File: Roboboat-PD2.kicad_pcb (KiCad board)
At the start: 2 copper layers, 78 x 60.7 mm, 44 parts, among them J1 14.4V, J10 Motor, J11 Motor, J12 Motor, J13 Motor, J14 Motor, J15 Motor, J16 Motor, J17 GND TP, J2 PGOOD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

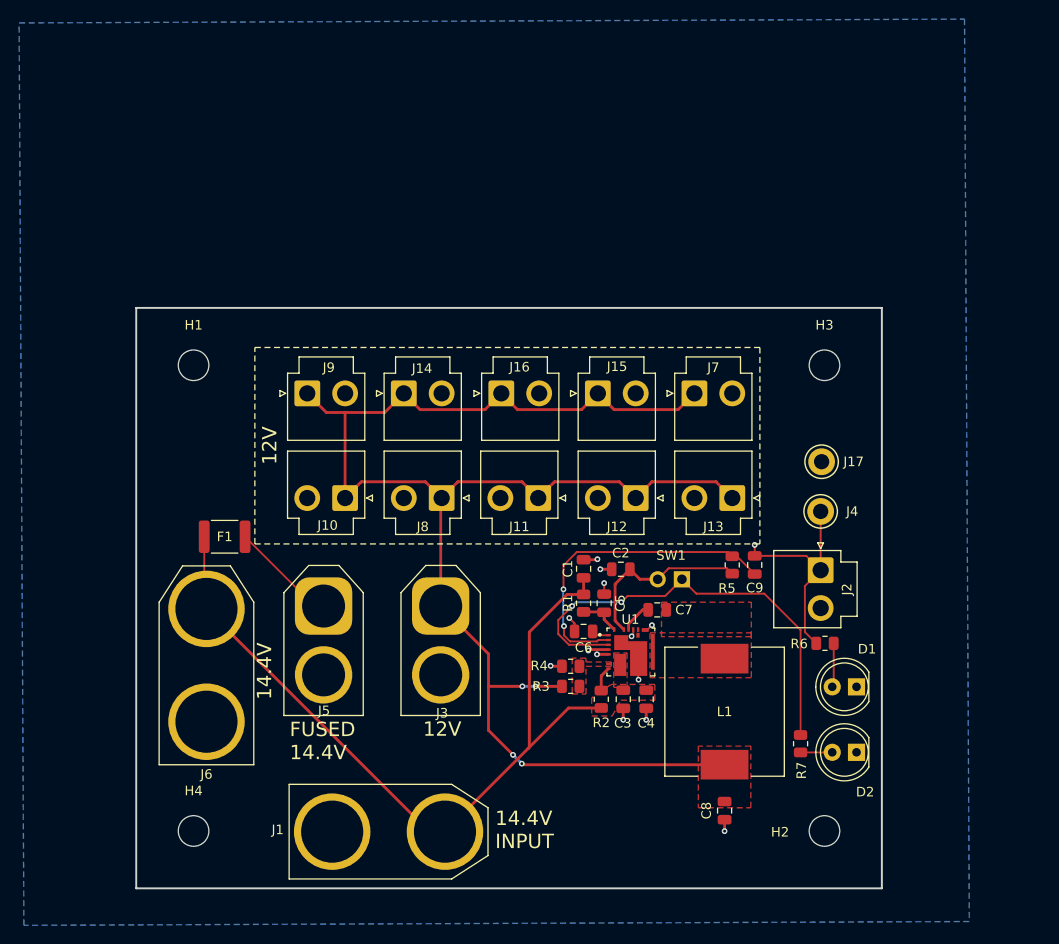
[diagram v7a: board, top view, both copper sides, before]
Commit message: add more test points
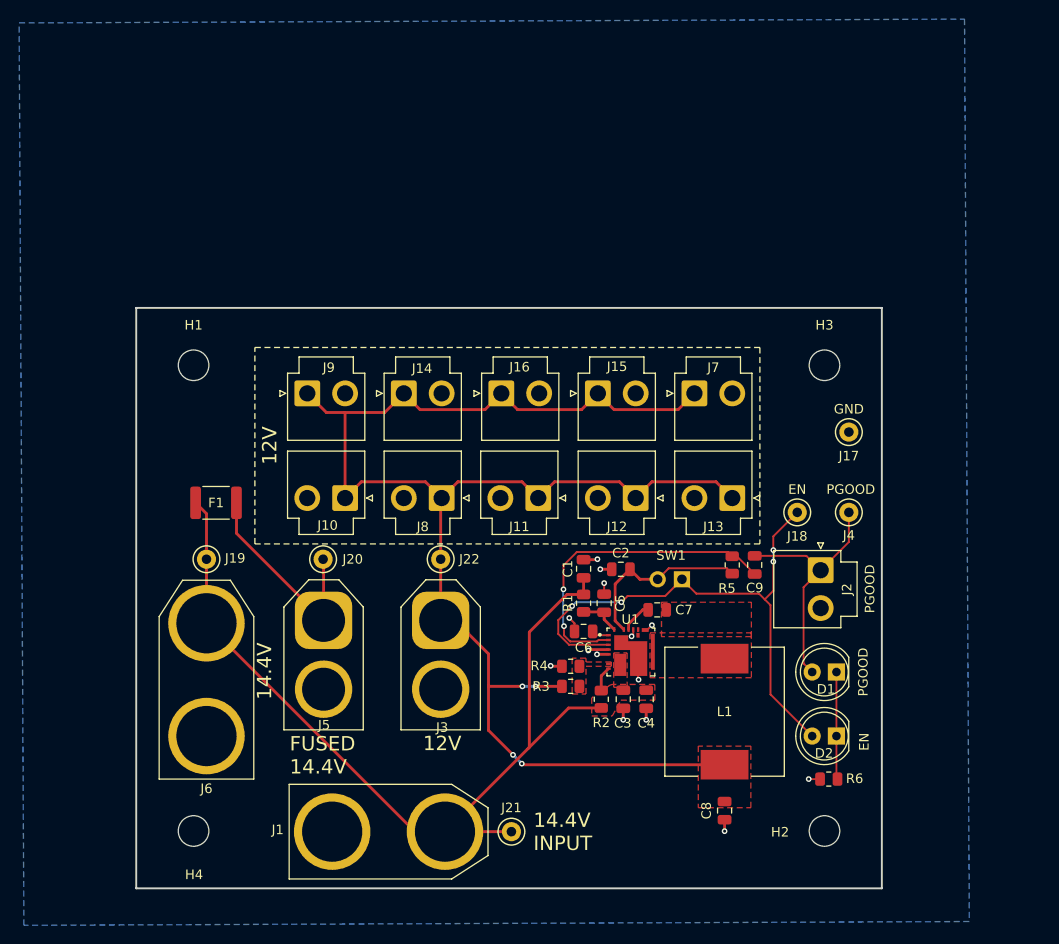
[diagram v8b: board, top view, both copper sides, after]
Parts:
- removed R7: 180, Resistor_SMD:R_0805_2012Metric
- added J18: PGOOD TP, TestPoint:TestPoint_Keystone_5000-5004_Miniature, F.Cu at (164.8, 104.0)
- added J19: PGOOD TP, TestPoint:TestPoint_Keystone_5000-5004_Miniature, F.Cu at (103.0, 108.9)
- added J20: PGOOD TP, TestPoint:TestPoint_Keystone_5000-5004_Miniature, F.Cu at (115.2, 108.9)
- added J21: PGOOD TP, TestPoint:TestPoint_Keystone_5000-5004_Miniature, F.Cu at (134.9, 137.4)
- added J22: PGOOD TP, TestPoint:TestPoint_Keystone_5000-5004_Miniature, F.Cu at (127.5, 108.9)
- D2: value BLUE LED -> GREEN
- J17, J4: footprint TestPoint:TestPoint_Keystone_5010-5014_Multipurpose -> TestPoint:TestPoint_Keystone_5000-5004_Miniature
- R6: value 180 -> 220
- moved G*** 52.7 mm to (158.0, 124.5)
- moved R6 14.2 mm to (168.1, 131.9), turned to 180 degrees
- moved J17 4.21 mm to (170.2, 95.6)
- moved F1 3.66 mm to (104.0, 103.0)
- moved J4 2.95 mm to (170.2, 104.0)
- moved D2 2.70 mm to (168.9, 127.4)
- moved D1 2.61 mm to (168.9, 120.7)
- moved J3 1.50 mm to (127.5, 115.3)
- moved J5 1.50 mm to (115.2, 115.3)
- moved J6 1.50 mm to (103.0, 121.5)
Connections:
- net Net-(J5-Pin_1) renamed /14.4_F
- D1 pad 1: GND -> Net-(D1-K)
- D1 pad 2: Net-(D1-A) -> /PGOOD
- D2 pad 1: GND -> Net-(D1-K)
- D2 pad 2: Net-(D2-A) -> /EN
- R6 pad 1: /PGOOD -> Net-(D1-K)
- R6 pad 2: Net-(D1-A) -> GND
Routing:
- net +14.4V: track 83.2 -> 97.0 mm
- net /14.4_F: track 10.3 -> 22.5 mm
- net Net-(D1-K): track 0.00 -> 11.1 mm
- net /EN: track 47.5 -> 58.3 mm, vias 2 -> 4
- net Net-(D1-A): track 4.61 -> 0.00 mm
- net Net-(D2-A): track 3.32 -> 0.00 mm
- net /PGOOD: track 23.6 -> 26.6 mm, vias 1 -> 0
- net +12V: track 161.7 -> 163.3 mm
- net GND: track 17.4 -> 18.6 mm, vias 13 -> 14
- net Net-(U1-SS): track 1.82 -> 1.25 mm
- net Net-(U1-PGOOD): track 33.9 -> 33.4 mm
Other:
- board text added: "EN"
- board text added: "GND"
- board text added: "GalaxSea 12V Power Distribution {dblquote}Frieren{dblquote} Rev. 2"
- board text added: "PGOOD"
- board text removed: "GalaxSea 12V Power Distribution PD2 {dblquote}Frieren{dblquote}"
